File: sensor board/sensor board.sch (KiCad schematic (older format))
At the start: 27 parts, among them IC1 AD5933YRSZ, IC2 MAX86141ENP+, J1 502078-1710, J2 Probe_01_male, J3 Probe_01_male, J4 Probe_01_male, J5 Probe_01_male

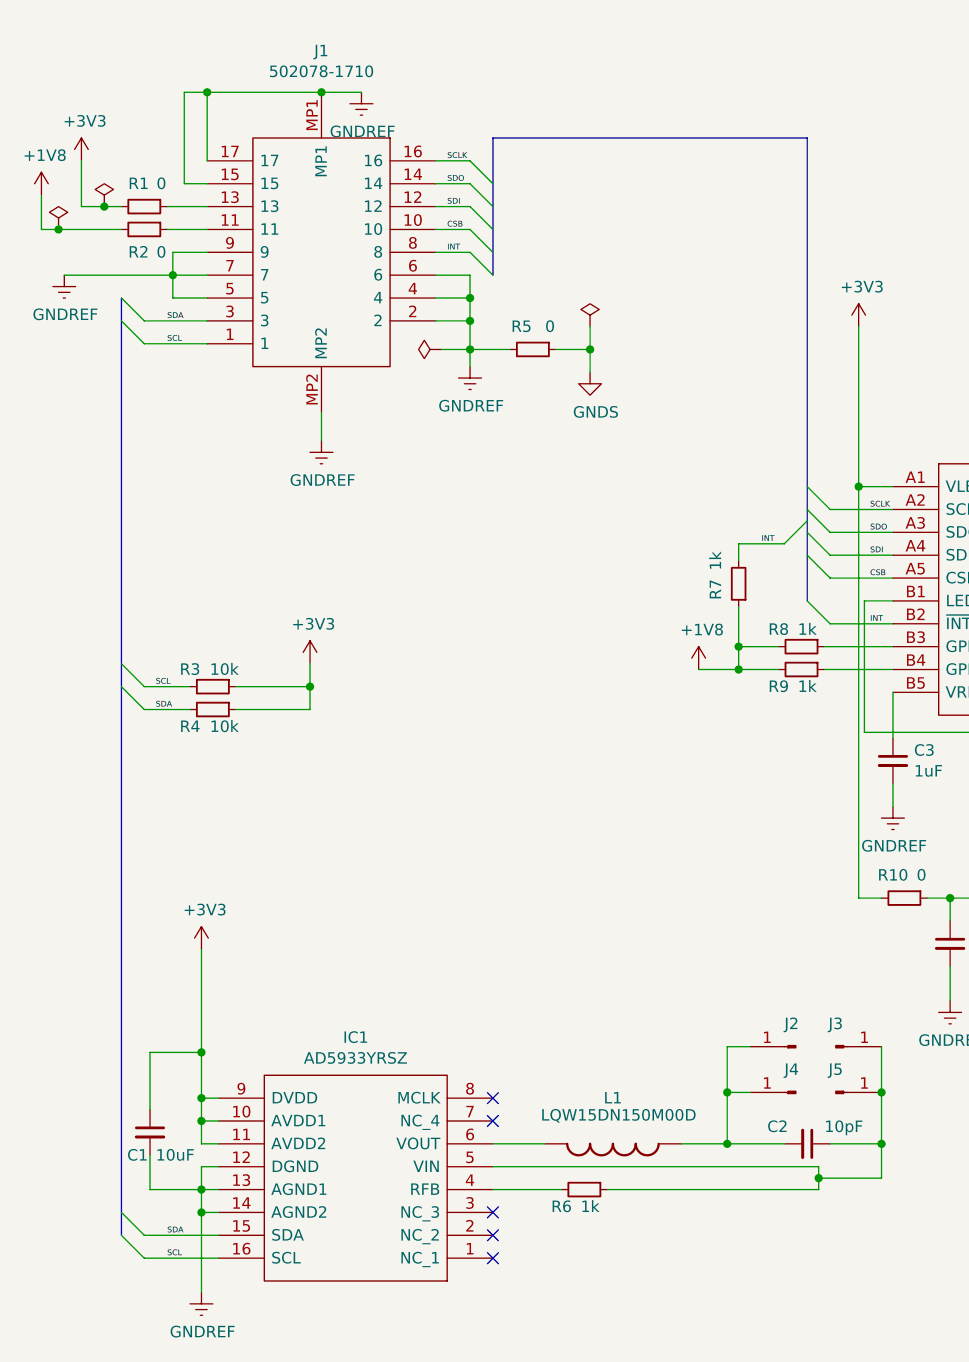
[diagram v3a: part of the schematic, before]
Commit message: finished sensor PCB
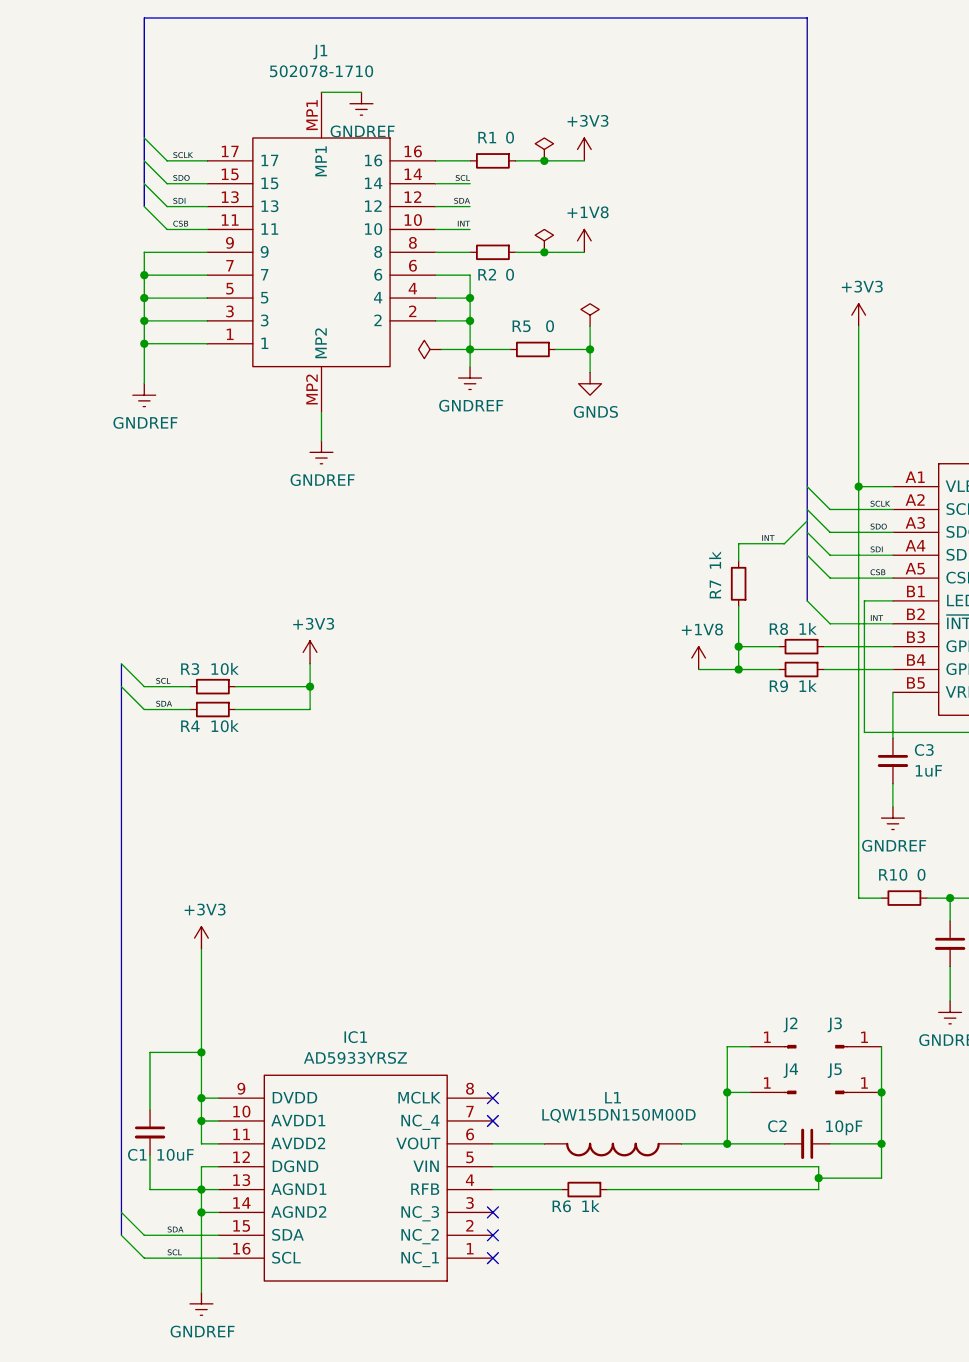
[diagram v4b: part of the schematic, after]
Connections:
- net +1V8: now also R2.1; no longer R2.2
- net +3V3: now also R1.1; no longer R1.2
- net CSB: now also J1.11; no longer J1.10
- net GNDREF: now also J1.1, J1.3; no longer J1.15, J1.17
- net INT: now also J1.10; no longer J1.8
- net SCL: now also J1.14; no longer J1.1
- net SCLK: now also J1.17; no longer J1.16
- net SDA: now also J1.12; no longer J1.3
- net SDI: now also J1.13; no longer J1.12
- net SDO: now also J1.15; no longer J1.14
- new net: J1.16, R1.2
- new net: J1.8, R2.2
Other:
- moved on the sheet: R1, R2
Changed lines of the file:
@@
 	0    1    1    0
 $EndComp
-Entry Wire Line
-	1275 2225 1375 2325
-Wire Wire Line
-	1375 2325 1650 2325
-Entry Wire Line
-	1275 2125 1375 2225
-Wire Wire Line
-	1375 2225 1650 2225
-Text Label 1475 2325 0    25   ~ 0
+Text Label 2800 1625 2    25   ~ 0
 SCL
-Text Label 1475 2225 0    25   ~ 0
+Text Label 2800 1725 2    25   ~ 0
 SDA
-Entry Wire Line
-	2800 1525 2900 1625
-Entry Wire Line
-	2800 1625 2900 1725
 Wire Wire Line
 	2650 1625 2800 1625
@@
 Wire Wire Line
 	10025 2950 10025 3850
-Entry Wire Line
-	2800 1825 2900 1925
-Entry Wire Line
-	2800 1725 2900 1825
-Entry Wire Line
-	2800 1925 2900 2025
 Wire Wire Line
 	2650 1725 2800 1725
@@
 Wire Wire Line
 	2650 1925 2800 1925
-Wire Bus Line
-	4275 1425 2900 1425
-Text Label 2700 1525 0    25   ~ 0
+Text Label 1500 1525 0    25   ~ 0
 SCLK
-Text Label 2700 1625 0    25   ~ 0
+Text Label 1500 1625 0    25   ~ 0
 SDO
-Text Label 2700 1725 0    25   ~ 0
+Text Label 1500 1725 0    25   ~ 0
 SDI
-Text Label 2700 1825 0    25   ~ 0
+Text Label 1500 1825 0    25   ~ 0
 CSB
-Text Label 2700 1925 0    25   ~ 0
+Text Label 2800 1825 2    25   ~ 0
 INT
 $Comp
@@
 Wire Wire Line
 	2150 1225 2325 1225
-Wire Wire Line
-	1650 1525 1650 1225
-Wire Wire Line
-	1650 1225 2150 1225
-Connection ~ 2150 1225
 Wire Wire Line
 	2900 6025 3200 6025
@@
 L power:+1V8 #PWR0117
 U 1 1 602D7956
-P 925 1675
-F 0 "#PWR0117" H 925 1525 50  0001 C CNN
-F 1 "+1V8" H 940 1848 50  0000 C CNN
-F 2 "" H 925 1675 50  0001 C CNN
-F 3 "" H 925 1675 50  0001 C CNN
-	1    925  1675
+P 3300 1925
+F 0 "#PWR0117" H 3300 1775 50  0001 C CNN
+F 1 "+1V8" H 3315 2098 50  0000 C CNN
+F 2 "" H 3300 1925 50  0001 C CNN
+F 3 "" H 3300 1925 50  0001 C CNN
+	1    3300 1925
 	1    0    0    -1
 $EndComp
@@
 L power:GNDREF #PWR0120
 U 1 1 602F8D56
-P 1025 2025
-F 0 "#PWR0120" H 1025 1775 50  0001 C CNN
-F 1 "GNDREF" H 1030 1852 50  0000 C CNN
-F 2 "" H 1025 2025 50  0001 C CNN
-F 3 "" H 1025 2025 50  0001 C CNN
-	1    1025 2025
-	1    0    0    -1
-$EndComp
-Wire Wire Line
-	1025 2025 1500 2025
-Wire Wire Line
-	1650 1925 1500 1925
-Wire Wire Line
-	1500 1925 1500 2025
-Connection ~ 1500 2025
-Wire Wire Line
-	1500 2025 1650 2025
-Wire Wire Line
-	1650 2125 1500 2125
-Wire Wire Line
-	1500 2025 1500 2125
+P 1375 2500
+F 0 "#PWR0120" H 1375 2250 50  0001 C CNN
+F 1 "GNDREF" H 1380 2327 50  0000 C CNN
+F 2 "" H 1375 2500 50  0001 C CNN
+F 3 "" H 1375 2500 50  0001 C CNN
+	1    1375 2500
+	1    0    0    -1
+$EndComp
 $Comp
 L power:PWR_FLAG #FLG0102
 U 1 1 60336395
-P 1200 1725
-F 0 "#FLG0102" H 1200 1800 50  0001 C CNN
-F 1 "PWR_FLAG" H 1200 1898 50  0001 C CNN
-F 2 "" H 1200 1725 50  0001 C CNN
-F 3 "~" H 1200 1725 50  0001 C CNN
-	1    1200 1725
+P 3125 1525
+F 0 "#FLG0102" H 3125 1600 50  0001 C CNN
+F 1 "PWR_FLAG" H 3125 1698 50  0001 C CNN
+F 2 "" H 3125 1525 50  0001 C CNN
+F 3 "~" H 3125 1525 50  0001 C CNN
+	1    3125 1525
 	1    0    0    -1
 $EndComp
@@
 	1    0    0    -1
 $EndComp
-Wire Wire Line
-	1650 1625 1550 1625
-Wire Wire Line
-	1550 1625 1550 1225
-Wire Wire Line
-	1550 1225 1650 1225
-Connection ~ 1650 1225
 $Comp
 L Device:R_Small R5
@@
 L power:+3V3 #PWR0109
 U 1 1 6015B59F
-P 1100 1525
-F 0 "#PWR0109" H 1100 1375 50  0001 C CNN
-F 1 "+3V3" H 1115 1698 50  0000 C CNN
-F 2 "" H 1100 1525 50  0001 C CNN
-F 3 "" H 1100 1525 50  0001 C CNN
-	1    1100 1525
+P 3300 1525
+F 0 "#PWR0109" H 3300 1375 50  0001 C CNN
+F 1 "+3V3" H 3315 1698 50  0000 C CNN
+F 2 "" H 3300 1525 50  0001 C CNN
+F 3 "" H 3300 1525 50  0001 C CNN
+	1    3300 1525
 	1    0    0    -1
 $EndComp
@@
 L power:PWR_FLAG #FLG0101
 U 1 1 6001CA27
-P 1000 1825
-F 0 "#FLG0101" H 1000 1900 50  0001 C CNN
-F 1 "PWR_FLAG" H 950 1750 25  0001 C CNN
-F 2 "" H 1000 1825 50  0001 C CNN
-F 3 "~" H 1000 1825 50  0001 C CNN
-	1    1000 1825
+P 3125 1925
+F 0 "#FLG0101" H 3125 2000 50  0001 C CNN
+F 1 "PWR_FLAG" H 3075 1850 25  0001 C CNN
+F 2 "" H 3125 1925 50  0001 C CNN
+F 3 "~" H 3125 1925 50  0001 C CNN
+	1    3125 1925
 	1    0    0    -1
 $EndComp
@@
 L Device:R_Small R1
 U 1 1 6004118C
-P 1375 1725
-F 0 "R1" V 1275 1700 50  0000 C CNN
-F 1 "0" V 1275 1800 50  0000 C CNN
-F 2 "Resistor_SMD:R_0402_1005Metric" H 1375 1725 50  0001 C CNN
-F 3 "https://www.mouser.ee/datasheet/2/427/crcwce3-1762584.pdf" H 1375 1725 50  0001 C CNN
-F 4 "https://www.mouser.ee/ProductDetail/Vishay-Dale/CRCW04020000Z0EDC/?qs=sGAEpiMZZMvdGkrng054t0DrEhLhGh8gwkqbMx2gSI%252BmKUnjnIW1MQ%3D%3D" V 1375 1725 50  0001 C CNN "Mouser Price/Stock"
-F 5 "541-4062-2-ND" V 1375 1725 50  0001 C CNN "Digikey Part Number"
-F 6 "0.09" V 1375 1725 50  0001 C CNN "Price"
-	1    1375 1725
+P 2900 1525
+F 0 "R1" V 2800 1500 50  0000 C CNN
+F 1 "0" V 2800 1600 50  0000 C CNN
+F 2 "Resistor_SMD:R_0402_1005Metric" H 2900 1525 50  0001 C CNN
+F 3 "https://www.mouser.ee/datasheet/2/427/crcwce3-1762584.pdf" H 2900 1525 50  0001 C CNN
+F 4 "https://www.mouser.ee/ProductDetail/Vishay-Dale/CRCW04020000Z0EDC/?qs=sGAEpiMZZMvdGkrng054t0DrEhLhGh8gwkqbMx2gSI%252BmKUnjnIW1MQ%3D%3D" V 2900 1525 50  0001 C CNN "Mouser Price/Stock"
+F 5 "541-4062-2-ND" V 2900 1525 50  0001 C CNN "Digikey Part Number"
+F 6 "0.09" V 2900 1525 50  0001 C CNN "Price"
+	1    2900 1525
 	0    1    1    0
 $EndComp
@@
 L Device:R_Small R2
 U 1 1 6004B6CE
-P 1375 1825
-F 0 "R2" V 1475 1800 50  0000 C CNN
-F 1 "0" V 1475 1900 50  0000 C CNN
-F 2 "Resistor_SMD:R_0402_1005Metric" H 1375 1825 50  0001 C CNN
-F 3 "https://www.mouser.ee/datasheet/2/427/crcwce3-1762584.pdf" H 1375 1825 50  0001 C CNN
-F 4 "https://www.mouser.ee/ProductDetail/Vishay-Dale/CRCW04020000Z0EDC/?qs=sGAEpiMZZMvdGkrng054t0DrEhLhGh8gwkqbMx2gSI%252BmKUnjnIW1MQ%3D%3D" V 1375 1825 50  0001 C CNN "Mouser Price/Stock"
-F 5 "541-4062-2-ND" V 1375 1825 50  0001 C CNN "Digikey Part Number"
-F 6 "0.09" V 1375 1825 50  0001 C CNN "Price"
-	1    1375 1825
+P 2900 1925
+F 0 "R2" V 3000 1900 50  0000 C CNN
+F 1 "0" V 3000 2000 50  0000 C CNN
+F 2 "Resistor_SMD:R_0402_1005Metric" H 2900 1925 50  0001 C CNN
+F 3 "https://www.mouser.ee/datasheet/2/427/crcwce3-1762584.pdf" H 2900 1925 50  0001 C CNN
+F 4 "https://www.mouser.ee/ProductDetail/Vishay-Dale/CRCW04020000Z0EDC/?qs=sGAEpiMZZMvdGkrng054t0DrEhLhGh8gwkqbMx2gSI%252BmKUnjnIW1MQ%3D%3D" V 2900 1925 50  0001 C CNN "Mouser Price/Stock"
+F 5 "541-4062-2-ND" V 2900 1925 50  0001 C CNN "Digikey Part Number"
+F 6 "0.09" V 2900 1925 50  0001 C CNN "Price"
+	1    2900 1925
 	0    1    1    0
 $EndComp
 Wire Wire Line
-	1475 1825 1650 1825
-Wire Wire Line
 	1475 1725 1650 1725
-Wire Wire Line
-	1100 1525 1100 1725
-Wire Wire Line
-	1100 1725 1200 1725
-Wire Wire Line
-	925  1675 925  1825
-Wire Wire Line
-	925  1825 1000 1825
-Connection ~ 1200 1725
-Wire Wire Line
-	1200 1725 1275 1725
-Connection ~ 1000 1825
-Wire Wire Line
-	1000 1825 1275 1825
 $Comp
 L Device:R_Small R10
@@
 Wire Wire Line
 	6150 3150 6225 3150
-Wire Bus Line
-	2900 1425 2900 2025
-Wire Bus Line
-	4275 1425 4275 3450
-Wire Bus Line
-	1275 2125 1275 6225
 Connection ~ 6500 3350
 Wire Wire Line
@@
 Wire Wire Line
 	6225 3150 6500 3150
+Wire Wire Line
+	3000 1525 3125 1525
+Connection ~ 3125 1525
+Wire Wire Line
+	3125 1525 3300 1525
+Entry Wire Line
+	1375 1625 1475 1725
+Entry Wire Line
+	1375 1725 1475 1825
+Wire Wire Line
+	1475 1825 1650 1825
+Wire Wire Line
+	3000 1925 3125 1925
+Connection ~ 3125 1925
+Wire Wire Line
+	3125 1925 3300 1925
+Wire Wire Line
+	1475 1625 1650 1625
+Wire Wire Line
+	1475 1525 1650 1525
+Wire Wire Line
+	1375 2500 1375 2325
+Wire Wire Line
+	1375 2225 1650 2225
+Connection ~ 1375 2225
+Wire Wire Line
+	1375 2225 1375 2125
+Wire Wire Line
+	1375 2325 1650 2325
+Connection ~ 1375 2325
+Wire Wire Line
+	1375 2325 1375 2225
+Wire Wire Line
+	1375 2025 1650 2025
+Wire Wire Line
+	1375 2125 1650 2125
+Connection ~ 1375 2125
+Wire Wire Line
+	1650 1925 1375 1925
+Wire Wire Line
+	1375 1925 1375 2025
+Connection ~ 1375 2025
+Wire Wire Line
+	1375 2025 1375 2125
+Entry Wire Line
+	1375 1425 1475 1525
+Entry Wire Line
+	1375 1525 1475 1625
+Wire Bus Line
+	1375 900  4275 900
+Wire Bus Line
+	1275 3725 1275 6225
+Wire Bus Line
+	1375 900  1375 1725
+Wire Bus Line
+	4275 900  4275 3450
 $EndSCHEMATC

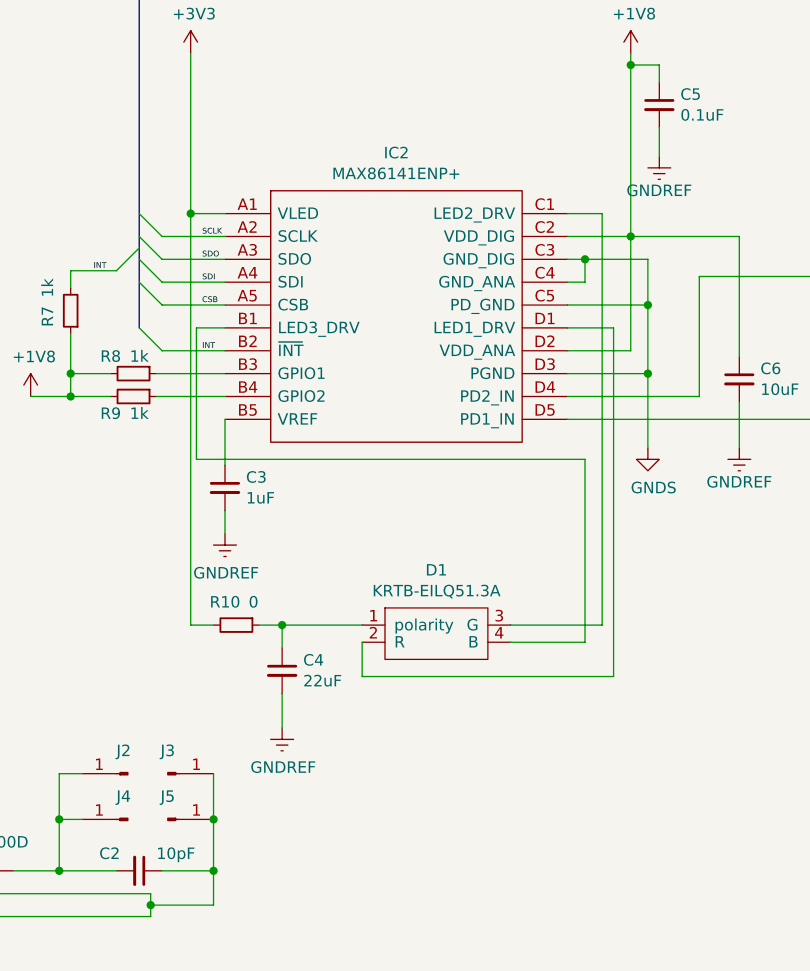
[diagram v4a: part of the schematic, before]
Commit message: replace LED, changed board layout and created files for production
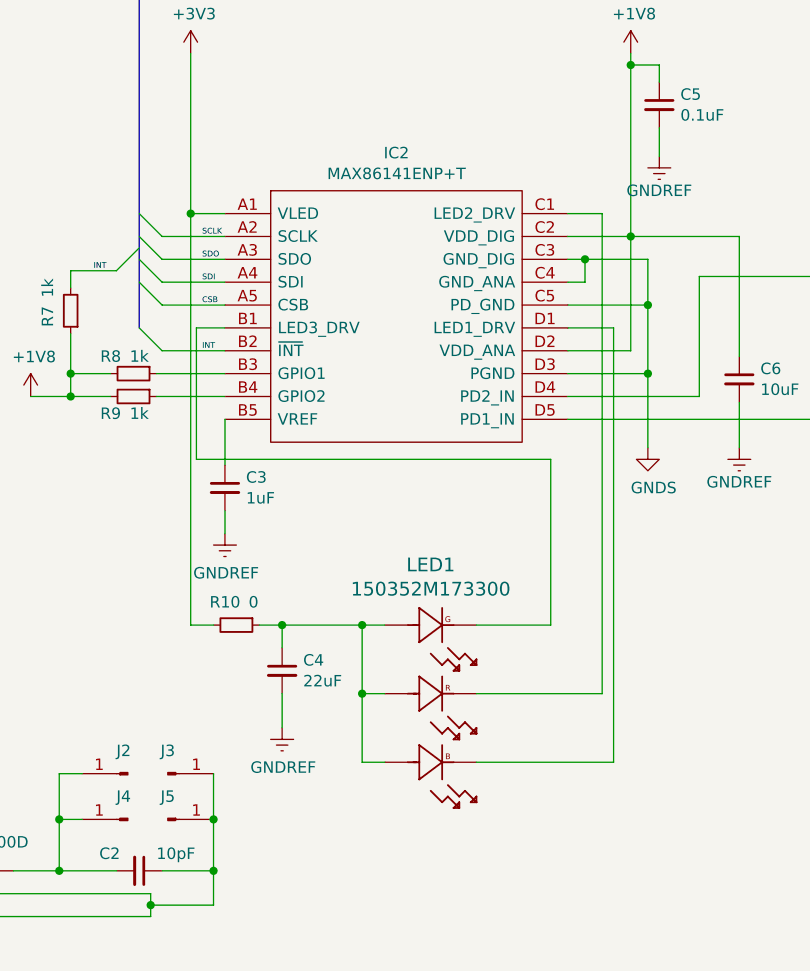
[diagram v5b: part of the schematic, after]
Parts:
- removed D1: KRTB-EILQ51.3A, Horace:KRTB-EILQ51.3A, symbol Horace:KRTB-EILQ51.3A
- added LED1: 150352M173300, Horace:150352M173300, symbol Horace:150352M173300
- C1, C6: Manufacturer (none) -> Yageo; Manufacturer Part Number (none) -> CC0402MRX5R5BB106
- C2: Manufacturer (none) -> Yageo; Manufacturer Part Number (none) -> CC0402FRNPO9BN100; Mouser Price/Stock https://www.mouser.ee/ProductDetail/Yageo/CC0402FRNPO9BN100/?qs=5q%252BqlK8CmJS9pmxsdlpWSg%3D%3 -> https://www.mouser.ee/ProductDetail/Yageo/CC0402FRNPO9BN100?qs=%2Fha2pyFaduht93PdrGJy4T4TiIbeqQQ85zpPRMvo9ZFqfthLvsVEgQ%3D%3D
- C3: Manufacturer (none) -> Yageo; Manufacturer Part Number (none) -> CC0402KRX5R5BB105
- C4: Manufacturer (none) -> Yageo; Manufacturer Part Number (none) -> CC0402MRX5R5BB226
- C5: Manufacturer (none) -> Yageo; Manufacturer Part Number (none) -> CC0402KRX5R5BB104
- D2, D3: Manufacturer (none) -> Vishay; Manufacturer Part Number (none) -> VEMD8080; Manufacturer_Name Vishay -> (none); Manufacturer_Part_Number VEMD8080 -> (none)
- IC1: Manufacturer (none) -> Analog Devices; Manufacturer Part Number (none) -> AD5933YRSZ; Manufacturer_Name Analog Devices -> (none); Manufacturer_Part_Number AD5933YRSZ -> (none)
- IC2: value MAX86141ENP+ -> MAX86141ENP+T; Digikey Part Number MAX86141ENP+-ND -> MAX86141ENP+TCT-ND; Manufacturer (none) -> Maxim Integrated; Manufacturer Part Number (none) -> MAX86141ENP+T; Manufacturer_Name Maxim Integrated -> (none); Manufacturer_Part_Number MAX86141ENP+ -> (none); Mouser Part Number 700-MAX86141ENP+ -> 700-MAX86141ENP+T; Mouser Price/Stock https://www.mouser.co.uk/ProductDetail/Maxim-Integrated/MAX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 -> https://www.mouser.ee/ProductDetail/Maxim-Integrated/MAX861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; Price 6.77 -> 6.25
- J1: Manufacturer Name (none) -> Molex; Manufacturer Part Number (none) -> 502078-1710; Manufacturer_Name Molex -> (none); Manufacturer_Part_Number 502078-1710 -> (none)
- L1: Manufacturer (none) -> Murata Electronics; Manufacturer Part Number (none) -> LQW15DN150M00D; Manufacturer_Name Murata Electronics -> (none); Manufacturer_Part_Number LQW15DN150M00D -> (none)
- R1, R10, R2, R5: Manufacturer (none) -> Vishay / Dale; Manufacturer Part Number (none) -> CRCW04020000Z0EDC
- R3, R4: Manufacturer (none) -> Vishay / Dale; Manufacturer Part Number (none) -> CRCW010010K0JREL
- R6, R7, R8, R9: Manufacturer (none) -> Vishay / Dale; Manufacturer Part Number (none) -> CRCW01001K00JREL
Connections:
- net at C4.1, R10.1: now also LED1.2, LED1.4, LED1.6
- net at IC2.D1 (LED1_DRV): now also LED1.1
- net at IC2.C1 (LED2_DRV): now also LED1.3
- net at IC2.B1 (LED3_DRV): now also LED1.5

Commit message: fixed silk labels locations
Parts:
- IC1: footprint SOP65P780X200-16N -> Horace:SOP65P780X200-16N
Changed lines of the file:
@@
 F 0 "IC1" H 3500 5360 50  0000 C CNN
 F 1 "AD5933YRSZ" H 3500 5451 50  0000 C CNN
-F 2 "SOP65P780X200-16N" H 3950 6425 50  0001 L CNN
+F 2 "Horace:SOP65P780X200-16N" H 3950 6425 50  0001 L CNN
 F 3 "http://www.analog.com/static/imported-files/data_sheets/AD5933.pdf" H 3950 6325 50  0001 L CNN
 F 4 "AD5933YRSZ, Impedance Converter, 16-Pin SSOP" H 3950 6225 50  0001 L CNN "Description"
